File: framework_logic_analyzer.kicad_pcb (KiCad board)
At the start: 4 copper layers, 63 x 40.5 mm, 112 parts, among them IC1 TXU0104QWBQARQ1, IC2 TXU0104QWBQARQ1, IC3 TXU0104QWBQARQ1, IC4 TXU0104QWBQARQ1, IC5 CYUSB3014-BZXC, J3 Conn_ARM_JTAG_SWD_10, J4 6101XX249121_610108249121, J5 6101XX249121_610108249121, J6 6101XX249121_610108249121, J7 6101XX249121_610108249121, P1 USB_C_Receptacle, Q1 MMBT3904, Q2 MMBT3904, Q3 MMBT3904, U1 NCP360SNT1G, U2 WE-TVS-82400102, U3 AP2112K-3.3, U4 SC189CSKTRT, U5 M24M02-DR, Y1 19.200 MHz

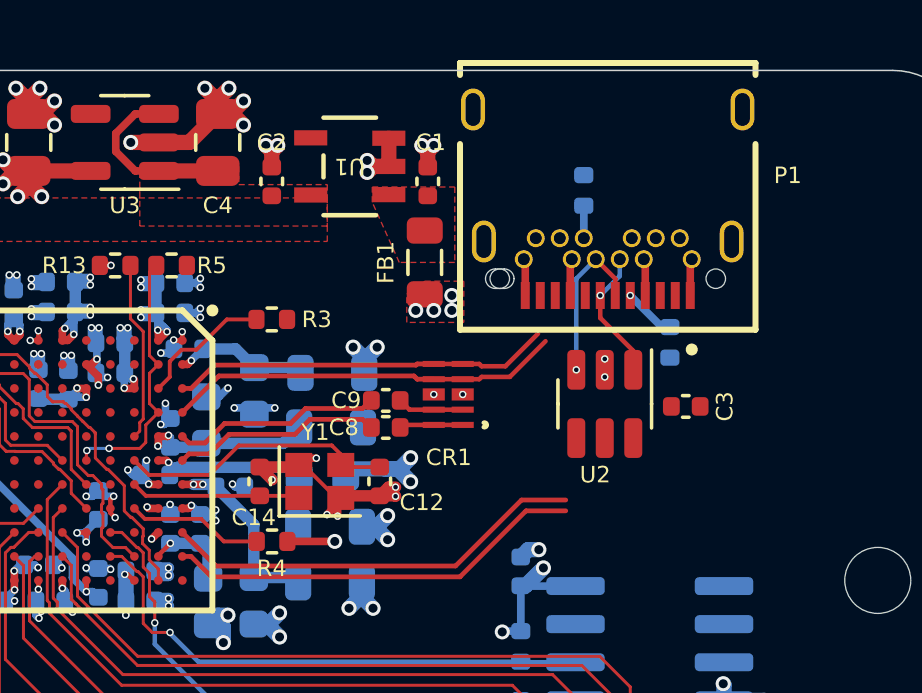
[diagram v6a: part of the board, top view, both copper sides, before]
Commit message: begin USB3 layouting ...
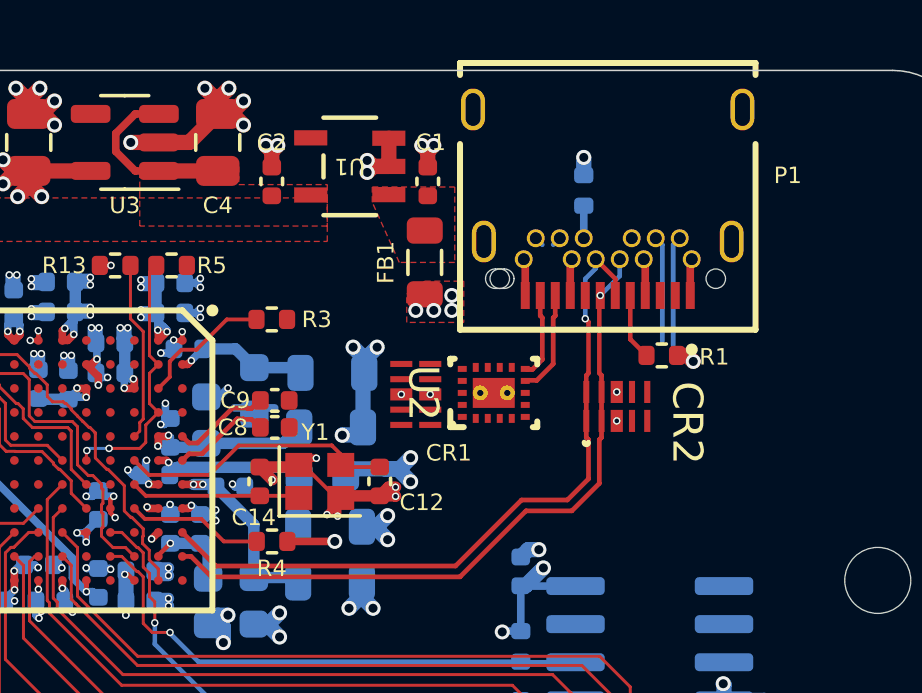
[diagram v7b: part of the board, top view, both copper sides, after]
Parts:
- removed C3: 100n, Capacitor_SMD:C_0402_1005Metric
- added CR2: SP3010-04UTG, SP3010:UDFEN-10_MO229_LTF, F.Cu at (156.2, 76.8)
- R1: moved to F.Cu
- U2: value WE-TVS-82400102 -> TUSB542RWQR; footprint Package_TO_SOT_SMD:SOT-23-6 -> Snapeda:RWQ0018A
- moved U2 3.72 mm to (152.1, 76.3), turned to 90 degrees
- moved C8 3.70 mm to (144.8, 77.5)
- moved C9 3.70 mm to (144.8, 76.6)
- moved CR1 1.08 mm to (149.5, 76.4)
- moved R1 0.51 mm to (157.7, 75.1), turned to 0 degrees
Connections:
- IC5 pad A10: /USB-C/SS_D- -> /USB-C/SSD-
- IC5 pad A9: /USB-C/SS_D+ -> /USB-C/SSD+
- P1 pad A10: /USB-C/SS_RX- -> /USB-C/SS_RX2-
- P1 pad A11: /USB-C/SS_RX+ -> /USB-C/SS_RX2+
- P1 pad A2: /USB-C/SS_TX+ -> /USB-C/SS_TX1+
- P1 pad A3: /USB-C/SS_TX- -> /USB-C/SS_TX1-
- P1 pad B10: /USB-C/SS_RX- -> /USB-C/SS_RX1-
- P1 pad B11: /USB-C/SS_RX+ -> /USB-C/SS_RX1+
- P1 pad B2: /USB-C/SS_TX+ -> /USB-C/SS_TX2+
- P1 pad B3: /USB-C/SS_TX- -> /USB-C/SS_TX2-
- U2 pad 1: /USB-C/SSD- -> unconnected-(U2-CNFG_A1-Pad1)
- U2 pad 2: GND -> /USB-C/SS_RX1+
- U2 pad 3: /USB-C/SSD+ -> /USB-C/SS_RX1-
- U2 pad 4: /USB-C/SS_D+ -> unconnected-(U2-CNFG_B1-Pad4)
- U2 pad 5: /USB-C/VBUS_IN -> unconnected-(U2-VDD18-Pad5)
- U2 pad 6: /USB-C/SS_D- -> /USB-C/SS_TX1+
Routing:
- net /USB-C/SSD-: track 4.41 -> 23.3 mm
- net /USB-C/SSD+: track 5.44 -> 24.3 mm
- net /USB-C/SS_D+: track 14.2 -> 0.00 mm
- net /USB-C/SS_D-: track 14.0 -> 0.00 mm
- net /USB-C/SS_RX+: track 13.2 -> 0.00 mm
- net /USB-C/SS_RX-: track 12.7 -> 0.00 mm
- net /SS_AC_TX+: track 6.98 -> 3.29 mm
- net /SS_AC_TX-: track 6.98 -> 3.29 mm
- net /USB-C/SS_RX1+: track 0.00 -> 3.67 mm
- net /USB-C/SS_RX1-: track 0.00 -> 3.52 mm
- net /USB-C/SS_RX2-: track 0.00 -> 3.48 mm
- net /USB-C/SS_RX2+: track 0.00 -> 2.88 mm
- net +1V2: track 19.9 -> 22.5 mm, vias 24 -> 25
- net /USB-C/SS_TX+: track 2.21 -> 0.00 mm
- net /USB-C/SS_TX-: track 2.12 -> 0.00 mm
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
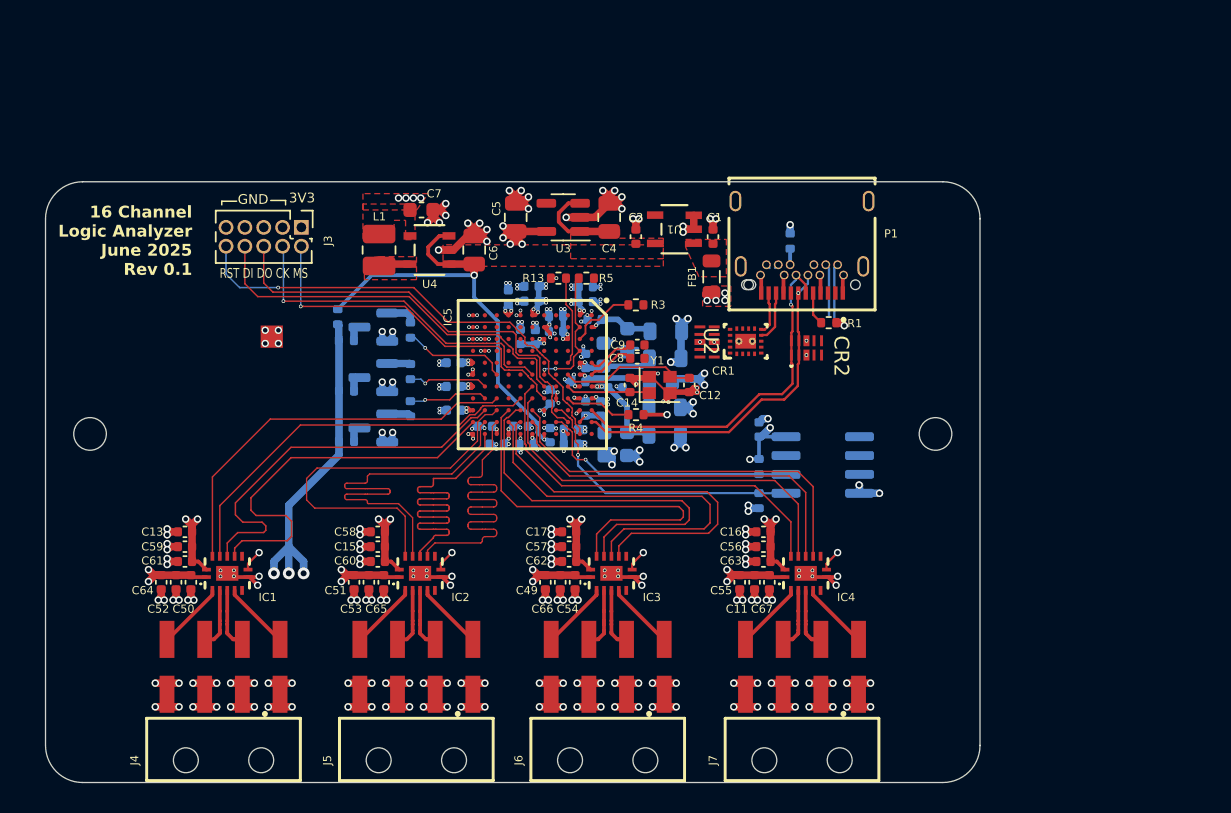
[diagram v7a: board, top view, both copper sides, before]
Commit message: add usb3 redriver
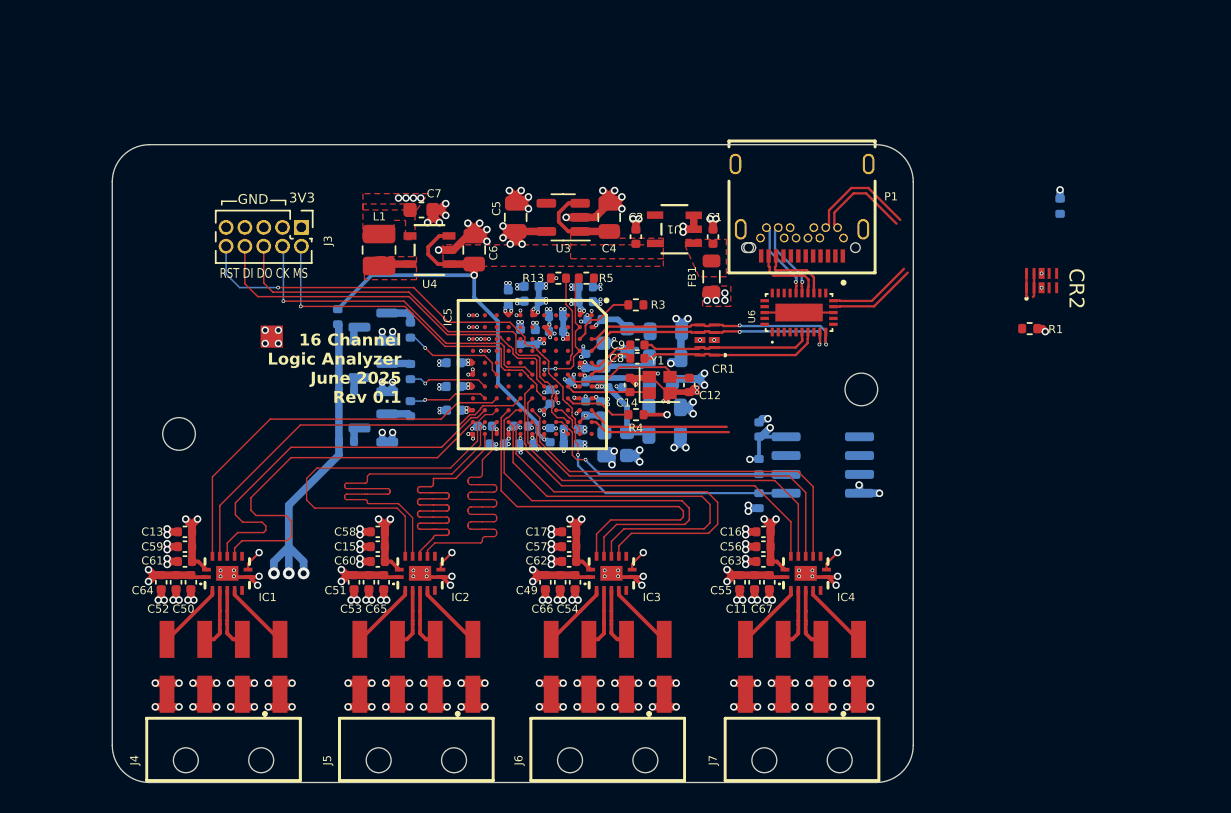
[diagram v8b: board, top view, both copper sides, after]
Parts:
- removed U2: TUSB542RWQR, Snapeda:RWQ0018A
- added U6: HD3SS3220IRNHT, Snapeda:HD3SS3220IRNHT_QFN40P450X250X80-31N120X320, F.Cu at (155.7, 74.4)
- moved R2 18.4 mm to (173.3, 67.2)
- moved CR2 16.5 mm to (172.1, 72.3)
- moved R1 13.6 mm to (171.2, 75.5)
- moved H1 6.00 mm to (113.9, 82.6)
- moved H2 5.83 mm to (159.9, 79.6)
- moved P1 2.50 mm to (155.9, 64.4)
- moved CR1 0.13 mm to (149.5, 76.3)
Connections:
- P1 pad A5: Net-(P1-CC1) -> /USB-C/CC1
- P1 pad B5: Net-(P1-CC2) -> /USB-C/CC2
- R1 pad 1: Net-(P1-CC1) -> unconnected-(R1-Pad1)
- R2 pad 1: Net-(P1-CC2) -> unconnected-(R2-Pad1)
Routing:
- net /USB-C/SS_RX-: track 0.00 -> 18.2 mm, vias 0 -> 2
- net /USB-C/SS_RX+: track 0.00 -> 17.8 mm, vias 0 -> 2
- net /USB-C/SSD+: track 24.3 -> 11.2 mm, vias 1 -> 0
- net /USB-C/SS_TX-: track 0.00 -> 12.3 mm
- net /USB-C/SSD-: track 23.3 -> 11.2 mm, vias 1 -> 0
- net /USB-C/SS_TX+: track 0.00 -> 11.6 mm
- net /USB-C/SS_RX1-: track 3.52 -> 13.5 mm
- net /USB-C/SS_RX1+: track 3.67 -> 12.3 mm
- net Net-(FB1-Pad1): track 11.2 -> 3.49 mm
- net /USB-C/SS_TX2-: track 0.31 -> 5.29 mm, vias 0 -> 1
- net /USB-C/SS_TX2+: track 0.31 -> 5.29 mm, vias 0 -> 1
- net Net-(P1-CC1): track 2.22 -> 0.00 mm
- net GND: track 169.9 -> 172.1 mm
- net /USB-C/SS_RX2+: track 2.88 -> 4.86 mm
- net /USB-C/SS_RX2-: track 3.48 -> 4.84 mm
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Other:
- board size 63 x 40.5 mm -> 54 x 43 mm
